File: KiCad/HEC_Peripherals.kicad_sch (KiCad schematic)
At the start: 13 parts, among them J2 Conn_02x12_Odd_Even, J6 DE9_Plug_MountingHoles, J7 AudioJack3, J8 NES_Port_Male, U43 74LS06, U44 74LS541, Y1 Crystal

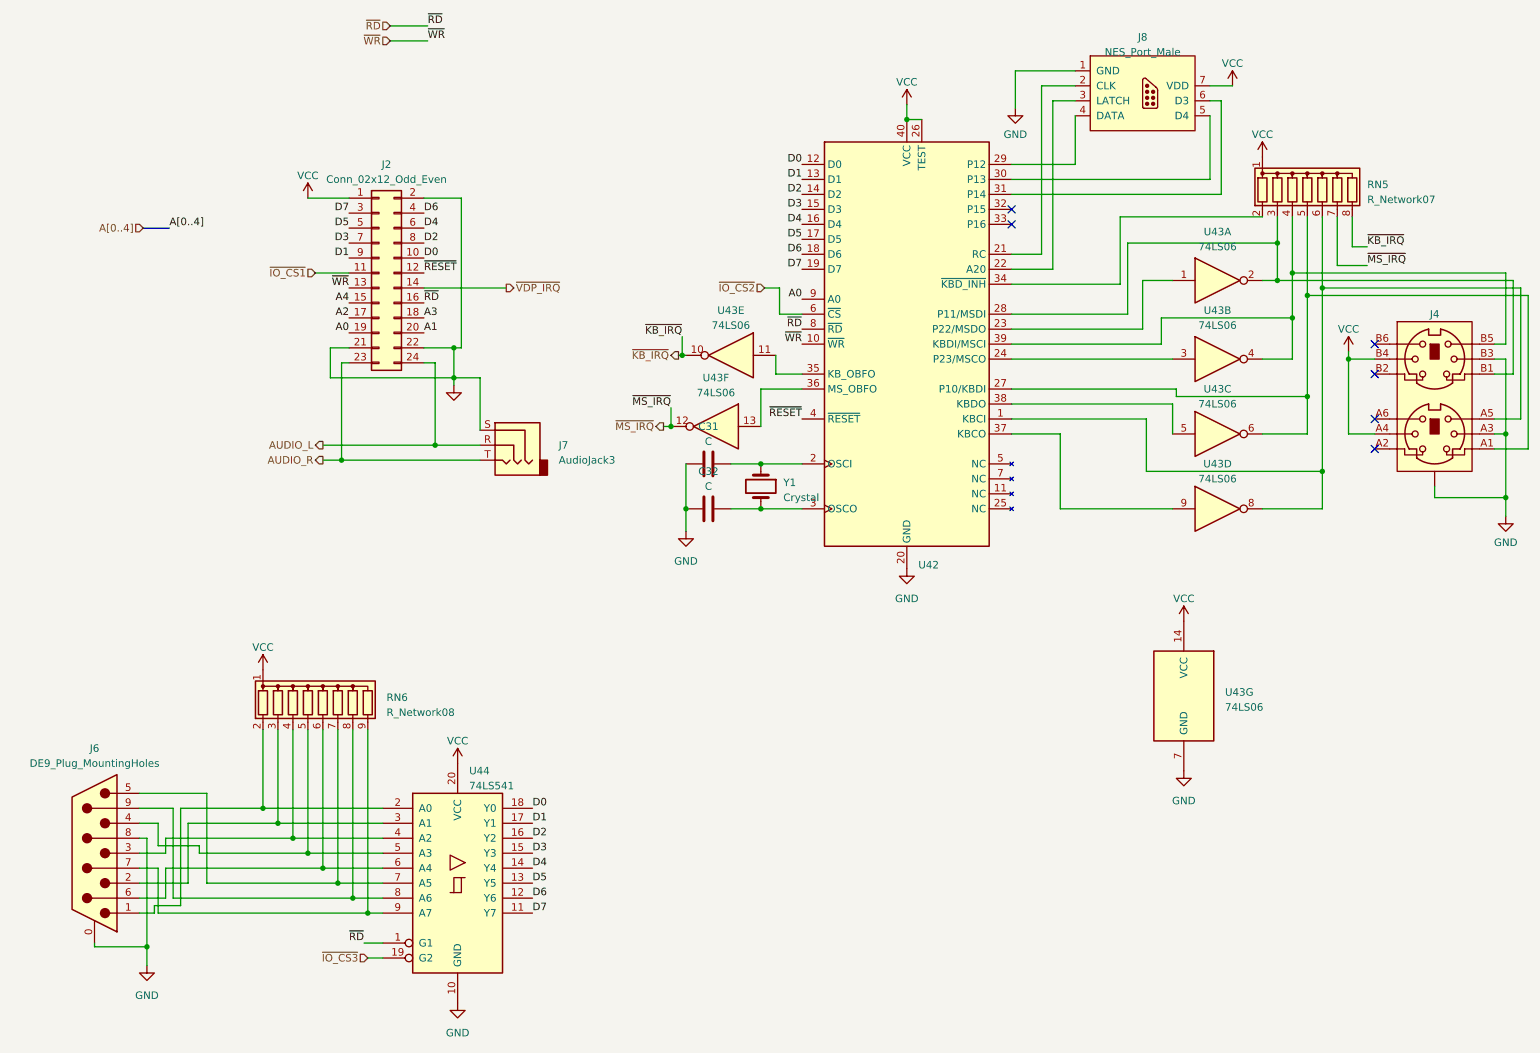
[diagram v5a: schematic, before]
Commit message: Preliminary layout
Very early stage layout prototype, very subject to change.
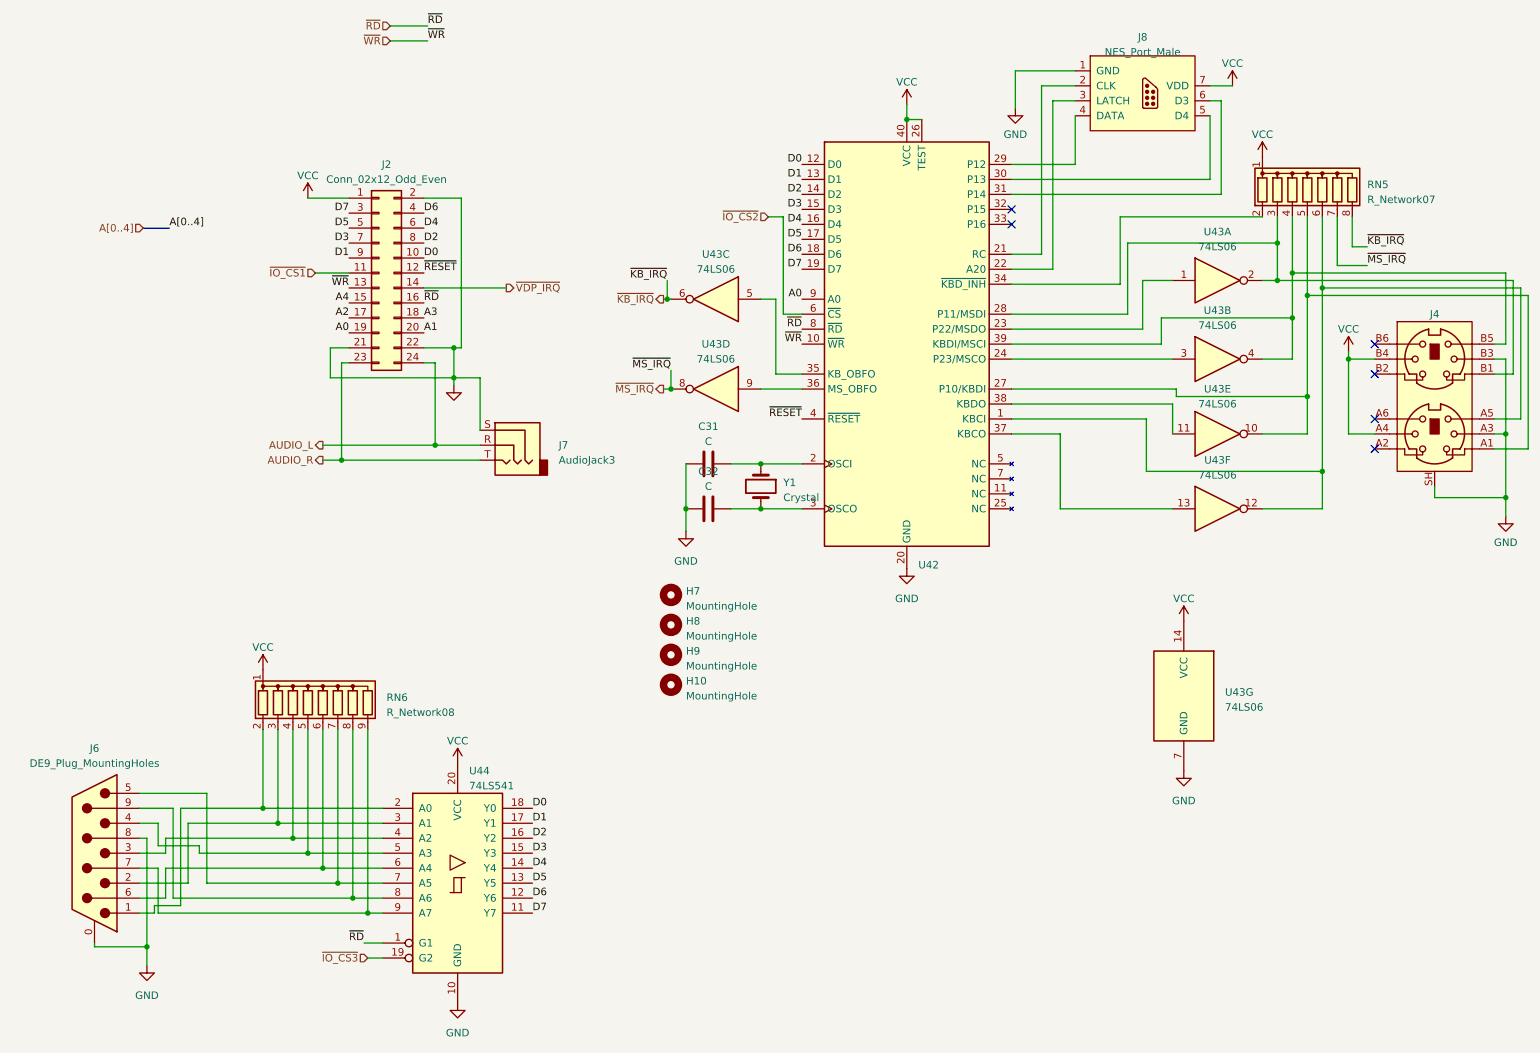
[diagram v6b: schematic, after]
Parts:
- added H10, H7, H8, H9: MountingHole, MountingHole:MountingHole_3.2mm_M3, symbol Mechanical:MountingHole
- J4: footprint (none) -> Library:Connector_double_mini-DIN_6
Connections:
- net GND: now also J4.SH; no longer J4.
- net ~{KB_IRQ}: now also U43.6; no longer U43.10
- net ~{MS_IRQ}: now also U43.8; no longer U43.12
- net at J4.A1, RN5.5 (R4), U42.27 (P10/KBDI): now also U43.10; no longer U43.6
- net at J4.A5, RN5.6 (R5), U42.1 (KBCI): now also U43.12; no longer U43.8
- net at U43.13: now also U42.37 (KBCO); no longer U42.36 (MS_OBFO)
- net at U43.9: now also U42.36 (MS_OBFO); no longer U42.37 (KBCO)
- net at U43.11: now also U42.38 (KBDO); no longer U42.35 (KB_OBFO)
- net at U43.5: now also U42.35 (KB_OBFO); no longer U42.38 (KBDO)
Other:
- moved on the sheet: U43C, U43D, U43E, U43F

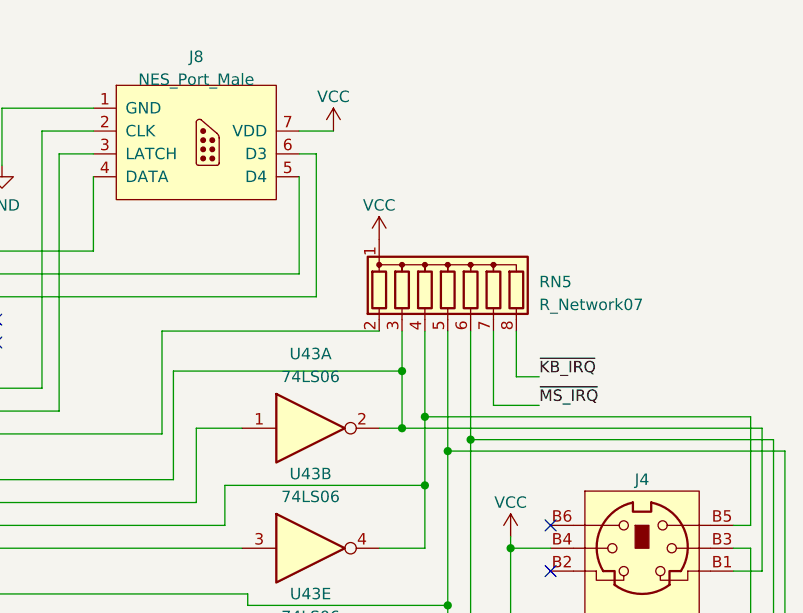
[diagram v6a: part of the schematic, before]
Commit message: More routing
Finished routing the IO part of the board. Currently it doesn't seem like a 4-layer board is needed.
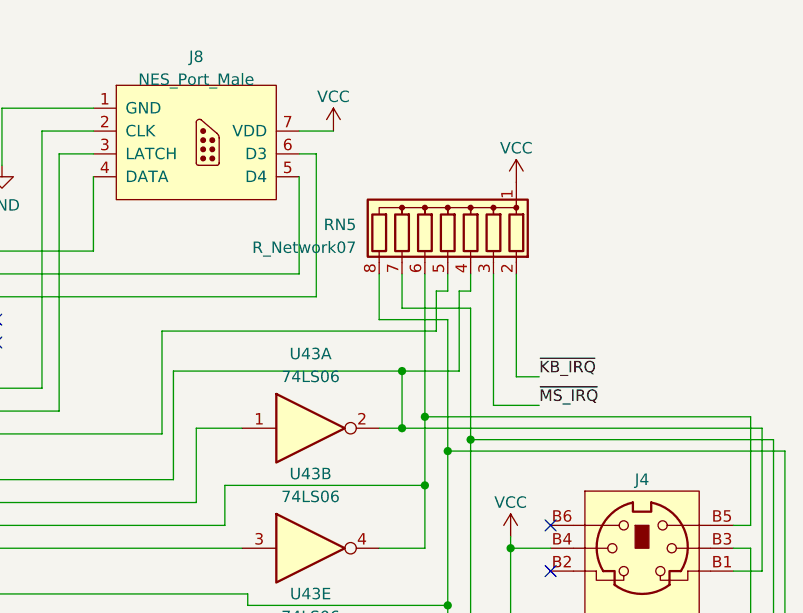
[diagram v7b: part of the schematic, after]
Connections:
- net ~{KB_IRQ}: now also RN5.2 (R1); no longer RN5.8 (R7)
- net ~{MS_IRQ}: now also RN5.3 (R2); no longer RN5.7 (R6)
- net at J4.A1, U42.27 (P10/KBDI), U43.10: now also RN5.8 (R7); no longer RN5.5 (R4)
- net at J4.A5, U42.1 (KBCI), U43.12: now also RN5.7 (R6); no longer RN5.6 (R5)
- net at J4.B1, U42.28 (P11/MSDI), U43.2: now also RN5.4 (R3); no longer RN5.3 (R2)
- net at J4.B5, U42.39 (KBDI/MSCI), U43.4: now also RN5.6 (R5); no longer RN5.4 (R3)
- net at U42.34 (~{KBD_INH}): now also RN5.5 (R4); no longer RN5.2 (R1)
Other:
- moved on the sheet: RN5
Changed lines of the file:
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@@
   (junction (at 241.3 97.79) (diameter 0) (color 0 0 0 0)
   )
+  (junction (at 241.3 66.675) (diameter 0) (color 0 0 0 0)
+  )
   (junction (at 236.22 64.135) (diameter 0) (color 0 0 0 0)
   )
@@
   (junction (at 133.35 104.14) (diameter 0) (color 0 0 0 0)
   )
+  (junction (at 61.595 154.94) (diameter 0) (color 0 0 0 0)
+  )
   (junction (at 233.68 59.055) (diameter 0) (color 0 0 0 0)
   )
-  (junction (at 61.595 154.94) (diameter 0) (color 0 0 0 0)
+  (junction (at 146.05 96.52) (diameter 0) (color 0 0 0 0)
+  )
+  (junction (at 93.98 81.915) (diameter 0) (color 0 0 0 0)
+  )
+  (junction (at 245.745 78.74) (diameter 0) (color 0 0 0 0)
+  )
+  (junction (at 238.76 85.09) (diameter 0) (color 0 0 0 0)
+  )
+  (junction (at 236.22 71.755) (diameter 0) (color 0 0 0 0)
+  )
+  (junction (at 130.175 68.58) (diameter 0) (color 0 0 0 0)
+  )
+  (junction (at 64.135 157.48) (diameter 0) (color 0 0 0 0)
   )
   (junction (at 238.76 67.945) (diameter 0) (color 0 0 0 0)
   )
-  (junction (at 146.05 96.52) (diameter 0) (color 0 0 0 0)
-  )
-  (junction (at 93.98 81.915) (diameter 0) (color 0 0 0 0)
-  )
-  (junction (at 245.745 78.74) (diameter 0) (color 0 0 0 0)
-  )
-  (junction (at 238.76 85.09) (diameter 0) (color 0 0 0 0)
-  )
-  (junction (at 236.22 71.755) (diameter 0) (color 0 0 0 0)
-  )
-  (junction (at 130.175 68.58) (diameter 0) (color 0 0 0 0)
-  )
-  (junction (at 64.135 157.48) (diameter 0) (color 0 0 0 0)
-  )
   (junction (at 233.68 65.405) (diameter 0) (color 0 0 0 0)
   )
   (junction (at 71.755 165.1) (diameter 0) (color 0 0 0 0)
-  )
-  (junction (at 241.3 66.675) (diameter 0) (color 0 0 0 0)
   )
   (junction (at 90.805 93.345) (diameter 0) (color 0 0 0 0)
@@
     (stroke (width 0) (type default))
   )
+  (wire (pts (xy 237.49 50.165) (xy 238.76 50.165))
+    (stroke (width 0) (type default))
+  )
   (wire (pts (xy 46.355 170.18) (xy 76.835 170.18))
     (stroke (width 0) (type default))
@@
     (stroke (width 0) (type default))
   )
+  (wire (pts (xy 238.76 50.165) (xy 238.76 48.26))
+    (stroke (width 0) (type default))
+  )
   (wire (pts (xy 76.835 170.18) (xy 81.915 170.18))
     (stroke (width 0) (type default))
@@
     (stroke (width 0) (type default))
   )
+  (wire (pts (xy 238.76 53.34) (xy 231.14 53.34))
+    (stroke (width 0) (type default))
+  )
+  (wire (pts (xy 241.3 50.165) (xy 241.3 48.26))
+    (stroke (width 0) (type default))
+  )
   (wire (pts (xy 270.51 88.9) (xy 274.955 88.9))
     (stroke (width 0) (type default))
@@
     (stroke (width 0) (type default))
   )
+  (wire (pts (xy 240.03 50.165) (xy 241.3 50.165))
+    (stroke (width 0) (type default))
+  )
   (wire (pts (xy 236.22 71.755) (xy 236.22 78.74))
     (stroke (width 0) (type default))
@@
     (stroke (width 0) (type default))
   )
+  (wire (pts (xy 240.03 59.055) (xy 240.03 50.165))
+    (stroke (width 0) (type default))
+  )
   (wire (pts (xy 41.91 178.435) (xy 33.02 178.435))
     (stroke (width 0) (type default))
@@
     (stroke (width 0) (type default))
   )
+  (wire (pts (xy 241.3 52.07) (xy 233.68 52.07))
+    (stroke (width 0) (type default))
+  )
   (wire (pts (xy 93.98 81.915) (xy 93.98 83.185))
     (stroke (width 0) (type default))
@@
     (stroke (width 0) (type default))
   )
+  (wire (pts (xy 238.76 67.945) (xy 238.76 53.34))
+    (stroke (width 0) (type default))
+  )
   (wire (pts (xy 74.295 141.605) (xy 74.295 167.64))
     (stroke (width 0) (type default))
@@
     (stroke (width 0) (type default))
   )
-  (wire (pts (xy 246.38 59.69) (xy 246.38 54.61))
+  (wire (pts (xy 246.38 48.26) (xy 246.38 59.69))
     (stroke (width 0) (type default))
   )
@@
     (stroke (width 0) (type default))
   )
-  (wire (pts (xy 243.84 54.61) (xy 243.84 62.865))
+  (wire (pts (xy 243.84 48.26) (xy 243.84 62.865))
     (stroke (width 0) (type default))
   )
@@
     (stroke (width 0) (type default))
   )
-  (wire (pts (xy 207.01 54.61) (xy 231.14 54.61))
+  (wire (pts (xy 207.01 54.61) (xy 237.49 54.61))
     (stroke (width 0) (type default))
   )
@@
     (stroke (width 0) (type default))
   )
-  (wire (pts (xy 238.76 54.61) (xy 238.76 67.945))
-    (stroke (width 0) (type default))
-  )
   (wire (pts (xy 40.64 157.48) (xy 43.815 157.48))
     (stroke (width 0) (type default))
   )
+  (wire (pts (xy 237.49 54.61) (xy 237.49 50.165))
+    (stroke (width 0) (type default))
+  )
   (wire (pts (xy 272.415 91.44) (xy 272.415 102.235))
     (stroke (width 0) (type default))
   )
-  (wire (pts (xy 241.3 54.61) (xy 241.3 66.675))
+  (wire (pts (xy 241.3 66.675) (xy 241.3 52.07))
     (stroke (width 0) (type default))
   )
@@
     (stroke (width 0) (type default))
   )
+  (wire (pts (xy 233.68 59.055) (xy 240.03 59.055))
+    (stroke (width 0) (type default))
+  )
   (wire (pts (xy 140.97 96.52) (xy 146.05 96.52))
     (stroke (width 0) (type default))
@@
     (stroke (width 0) (type default))
   )
-  (wire (pts (xy 233.68 54.61) (xy 233.68 59.055))
-    (stroke (width 0) (type default))
-  )
   (wire (pts (xy 260.35 100.33) (xy 260.35 102.235))
     (stroke (width 0) (type default))
@@
     (stroke (width 0) (type default))
   )
-  (wire (pts (xy 236.22 54.61) (xy 236.22 64.135))
+  (wire (pts (xy 236.22 48.26) (xy 236.22 64.135))
     (stroke (width 0) (type default))
   )
@@
     (stroke (width 0) (type default))
   )
+  (wire (pts (xy 233.68 52.07) (xy 233.68 48.26))
+    (stroke (width 0) (type default))
+  )
   (wire (pts (xy 83.185 22.225) (xy 89.535 22.225))
     (stroke (width 0) (type default))
@@
   )
   (wire (pts (xy 276.225 93.98) (xy 276.225 67.945))
+    (stroke (width 0) (type default))
+  )
+  (wire (pts (xy 231.14 53.34) (xy 231.14 48.26))
     (stroke (width 0) (type default))
   )
@@
     )
   )
-  (symbol (lib_id "power:VCC") (at 231.14 44.45 0) (unit 1)
+  (symbol (lib_id "power:VCC") (at 246.38 38.1 0) (mirror y) (unit 1)
     (in_bom yes) (on_board yes) (dnp no) (fields_autoplaced)
-    (property "Reference" "#PWR0118" (at 231.14 48.26 0)
-      (effects (font (size 1.27 1.27)) hide)
-    )
-    (property "Value" "VCC" (at 231.14 40.64 0)
+    (property "Reference" "#PWR0118" (at 246.38 41.91 0)
+      (effects (font (size 1.27 1.27)) hide)
+    )
+    (property "Value" "VCC" (at 246.38 34.29 0)
       (effects (font (size 1.27 1.27)))
     )
-    (property "Footprint" "" (at 231.14 44.45 0)
-      (effects (font (size 1.27 1.27)) hide)
-    )
-    (property "Datasheet" "" (at 231.14 44.45 0)
+    (property "Footprint" "" (at 246.38 38.1 0)
+      (effects (font (size 1.27 1.27)) hide)
+    )
+    (property "Datasheet" "" (at 246.38 38.1 0)
       (effects (font (size 1.27 1.27)) hide)
     )
@@
     )
   )
-  (symbol (lib_id "Device:R_Network07") (at 238.76 49.53 0) (unit 1)
+  (symbol (lib_id "Device:R_Network07") (at 238.76 43.18 0) (mirror y) (unit 1)
     (in_bom yes) (on_board yes) (dnp no) (fields_autoplaced)
-    (property "Reference" "RN5" (at 248.92 49.149 0)
+    (property "Reference" "RN5" (at 228.6 42.799 0)
       (effects (font (size 1.27 1.27)) (justify left))
     )
-    (property "Value" "R_Network07" (at 248.92 51.689 0)
+    (property "Value" "R_Network07" (at 228.6 45.339 0)
       (effects (font (size 1.27 1.27)) (justify left))
     )
-    (property "Footprint" "Resistor_THT:R_Array_SIP8" (at 250.825 49.53 90)
-      (effects (font (size 1.27 1.27)) hide)
-    )
-    (property "Datasheet" "http://www.vishay.com/docs/31509/csc.pdf" (at 238.76 49.53 0)
-      (effects (font (size 1.27 1.27)) hide)
-    )
+    (property "Footprint" "Resistor_THT:R_Array_SIP8" (at 226.695 43.18 90)
+      (effects (font (size 1.27 1.27)) hide)
+    )
+    (property "Datasheet" "http://www.vishay.com/docs/31509/csc.pdf" (at 238.76 43.18 0)
+      (effects (font (size 1.27 1.27)) hide)
+    )

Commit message: Bug fixes
fixed some bugs introduced to the schematic. More routing.
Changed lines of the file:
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@@
+    (stroke (width 0) (type default))
+  )
+  (wire (pts (xy 83.185 27.305) (xy 89.535 27.305))
     (stroke (width 0) (type default))
   )
@@
     (stroke (width 0) (type default))
   )
+  (bus (pts (xy 41.275 59.055) (xy 45.72 59.055))
+    (stroke (width 0) (type default))
+  )
   (wire (pts (xy 41.91 178.435) (xy 33.02 178.435))
     (stroke (width 0) (type default))
@@
     (effects (font (size 1.27 1.27)) (justify left bottom))
   )
+  (label "~{RESET}" (at 89.535 27.305 0) (fields_autoplaced)
+    (effects (font (size 1.27 1.27)) (justify left bottom))
+  )
   (label "~{KB_IRQ}" (at 248.92 59.69 0) (fields_autoplaced)
     (effects (font (size 1.27 1.27)) (justify left bottom))
@@
     (effects (font (size 1.27 1.27)) (justify right bottom))
   )
+  (label "D[0..7]" (at 45.72 59.055 0) (fields_autoplaced)
+    (effects (font (size 1.27 1.27)) (justify left bottom))
+  )
   (label "D2" (at 153.035 50.8 180) (fields_autoplaced)
     (effects (font (size 1.27 1.27)) (justify right bottom))
@@
     (effects (font (size 1.27 1.27)) (justify right))
   )
+  (hierarchical_label "D[0..7]" (shape input) (at 41.275 59.055 180) (fields_autoplaced)
+    (effects (font (size 1.27 1.27)) (justify right))
+  )
   (hierarchical_label "~{WR}" (shape input) (at 83.185 24.765 180) (fields_autoplaced)
     (effects (font (size 1.27 1.27)) (justify right))
@@
     (effects (font (size 1.27 1.27)) (justify right))
   )
+  (hierarchical_label "~{RESET}" (shape input) (at 83.185 27.305 180) (fields_autoplaced)
+    (effects (font (size 1.27 1.27)) (justify right))
+  )
